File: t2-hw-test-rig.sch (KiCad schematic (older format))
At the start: 36 parts

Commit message: annotated
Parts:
- gave numbers to parts that had none: 36

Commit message: annotated, netlist
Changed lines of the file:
@@
 $EndComp
 $Comp
-L GND #PWR110
+L GND #PWR01
 U 1 1 5530823B
 P 5100 7500
-F 0 "#PWR110" H 5100 7250 50  0001 C CNN
+F 0 "#PWR01" H 5100 7250 50  0001 C CNN
 F 1 "GND" H 5100 7350 50  0000 C CNN
 F 2 "" H 5100 7500 60  0000 C CNN
@@
 $EndComp
 $Comp
-L GND #PWR104
+L GND #PWR02
 U 1 1 553082CD
 P 3500 7500
-F 0 "#PWR104" H 3500 7250 50  0001 C CNN
+F 0 "#PWR02" H 3500 7250 50  0001 C CNN
 F 1 "GND" H 3500 7350 50  0000 C CNN
 F 2 "" H 3500 7500 60  0000 C CNN
@@
 $EndComp
 $Comp
-L GND #PWR106
+L GND #PWR03
 U 1 1 55308387
 P 3900 7000
-F 0 "#PWR106" H 3900 6750 50  0001 C CNN
+F 0 "#PWR03" H 3900 6750 50  0001 C CNN
 F 1 "GND" H 3900 6850 50  0000 C CNN
 F 2 "" H 3900 7000 60  0000 C CNN
@@
 $EndComp
 $Comp
-L GND #PWR108
+L GND #PWR04
 U 1 1 5530B320
 P 4400 5200
-F 0 "#PWR108" H 4400 4950 50  0001 C CNN
+F 0 "#PWR04" H 4400 4950 50  0001 C CNN
 F 1 "GND" H 4400 5050 50  0000 C CNN
 F 2 "" H 4400 5200 60  0000 C CNN
@@
 $EndComp
 $Comp
-L +5V #PWR101
+L +5V #PWR05
 U 1 1 5530BC5F
 P 3300 4800
-F 0 "#PWR101" H 3300 4650 50  0001 C CNN
+F 0 "#PWR05" H 3300 4650 50  0001 C CNN
 F 1 "+5V" H 3300 4940 50  0000 C CNN
 F 2 "" H 3300 4800 60  0000 C CNN
@@
 $EndComp
 $Comp
-L GND #PWR105
+L GND #PWR06
 U 1 1 5530C144
 P 3900 5700
-F 0 "#PWR105" H 3900 5450 50  0001 C CNN
+F 0 "#PWR06" H 3900 5450 50  0001 C CNN
 F 1 "GND" H 3900 5550 50  0000 C CNN
 F 2 "" H 3900 5700 60  0000 C CNN
@@
 $EndComp
 $Comp
-L GND #PWR103
+L GND #PWR07
 U 1 1 5530C207
 P 3500 5700
-F 0 "#PWR103" H 3500 5450 50  0001 C CNN
+F 0 "#PWR07" H 3500 5450 50  0001 C CNN
 F 1 "GND" H 3500 5550 50  0000 C CNN
 F 2 "" H 3500 5700 60  0000 C CNN
@@
 $EndComp
 $Comp
-L GND #PWR112
+L GND #PWR08
 U 1 1 5530C2A7
 P 6000 5700
-F 0 "#PWR112" H 6000 5450 50  0001 C CNN
+F 0 "#PWR08" H 6000 5450 50  0001 C CNN
 F 1 "GND" H 6000 5550 50  0000 C CNN
 F 2 "" H 6000 5700 60  0000 C CNN
@@
 $EndComp
 $Comp
-L +3.3V #PWR113
+L +3.3V #PWR09
 U 1 1 5530C581
 P 6300 4800
-F 0 "#PWR113" H 6300 4650 50  0001 C CNN
+F 0 "#PWR09" H 6300 4650 50  0001 C CNN
 F 1 "+3.3V" H 6300 4940 50  0000 C CNN
 F 2 "" H 6300 4800 60  0000 C CNN
@@
 $EndComp
 $Comp
-L +5V #PWR102
+L +5V #PWR010
 U 1 1 5536D76C
 P 3300 6600
-F 0 "#PWR102" H 3300 6450 50  0001 C CNN
+F 0 "#PWR010" H 3300 6450 50  0001 C CNN
 F 1 "+5V" H 3300 6740 50  0000 C CNN
 F 2 "" H 3300 6600 60  0000 C CNN
@@
 $EndComp
 $Comp
-L GND #PWR109
+L GND #PWR011
 U 1 1 5537EEAC
 P 5000 4000
-F 0 "#PWR109" H 5000 3750 50  0001 C CNN
+F 0 "#PWR011" H 5000 3750 50  0001 C CNN
 F 1 "GND" H 5000 3850 50  0000 C CNN
 F 2 "" H 5000 4000 60  0000 C CNN
@@
 $EndComp
 $Comp
-L +5V #PWR111
+L +5V #PWR012
 U 1 1 5537EEF8
 P 5400 2600
-F 0 "#PWR111" H 5400 2450 50  0001 C CNN
+F 0 "#PWR012" H 5400 2450 50  0001 C CNN
 F 1 "+5V" H 5400 2740 50  0000 C CNN
 F 2 "" H 5400 2600 60  0000 C CNN
@@
 	3500 6700 3500 6800
 Wire Wire Line
-	5000 6700 5100 6700
-Wire Wire Line
-	5100 6700 5300 6700
+	5000 6700 5300 6700
 Connection ~ 5100 6700
 Wire Wire Line
-	3300 6700 3500 6700
-Wire Wire Line
-	3500 6700 4000 6700
+	3300 6700 4000 6700
 Wire Wire Line
 	3900 7000 3900 6900
@@
 Connection ~ 3500 6700
 Wire Wire Line
-	3300 4900 3500 4900
-Wire Wire Line
-	3500 4900 3900 4900
-Wire Wire Line
-	3900 4900 4500 4900
+	3300 4900 4500 4900
 Wire Wire Line
 	3300 4900 3300 4800
 Wire Wire Line
-	5900 4900 6000 4900
-Wire Wire Line
-	6000 4900 6300 4900
+	5900 4900 6300 4900
 Wire Wire Line
 	4400 5200 4400 5100
@@
 	3300 6700 3300 6600
 Wire Wire Line
-	4200 3500 4400 3500
-Wire Wire Line
-	4400 3500 4800 3500
+	4200 3500 4800 3500
 Wire Wire Line
 	5400 3500 5200 3500
 Wire Wire Line
-	5400 2600 5400 2800
-Wire Wire Line
-	5400 2800 5400 3500
-Wire Wire Line
-	5000 3800 5000 3900
-Wire Wire Line
-	5000 3900 5000 4000
+	5400 2600 5400 3500
+Wire Wire Line
+	5000 3800 5000 4000
 Wire Wire Line
 	4200 3600 4300 3600
 Wire Wire Line
-	4300 3600 4300 3700
-Wire Wire Line
-	4300 3700 4300 3900
+	4300 3600 4300 3900
 Wire Wire Line
 	4300 3700 4200 3700
@@
 Connection ~ 4300 3700
 Wire Wire Line
-	4000 2800 4400 2800
-Wire Wire Line
-	4400 2800 4900 2800
+	4000 2800 4900 2800
 Wire Wire Line
 	4400 2800 4400 3500
 Connection ~ 4400 3500
 $Comp
-L GND #PWR107
+L GND #PWR013
 U 1 1 5537FB7D
 P 4100 3000
-F 0 "#PWR107" H 4100 2750 50  0001 C CNN
+F 0 "#PWR013" H 4100 2750 50  0001 C CNN
 F 1 "GND" H 4100 2850 50  0000 C CNN
 F 2 "" H 4100 3000 60  0000 C CNN

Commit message: components and footprints
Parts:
- C101: footprint (none) -> tm-kicad-lib:SMD-0805-C
- C102, C103, C104, C105: footprint (none) -> tm-kicad-lib:SMD-0402-C
- H101, H102, H103, H104: footprint (none) -> tm-kicad-lib:MountingHole_2-5mm
- J101, J103: footprint (none) -> Pin_Headers:Pin_Header_Straight_1x02
- J102: footprint (none) -> Connect:BARREL_JACK
- Q101: footprint FOOTPRINT -> Housings_SOT-23_SOT-143_TSOT-6:SOT-23
- U101, U102: footprint (none) -> Housings_SOT-23_SOT-143_TSOT-6:SOT-23
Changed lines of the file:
@@
 F 0 "C104" H 5125 7200 50  0000 L CNN
 F 1 "100nF" H 5125 7000 50  0000 L CNN
-F 2 "" H 5138 6950 30  0000 C CNN
+F 2 "tm-kicad-lib:SMD-0402-C" H 5138 6950 30  0001 C CNN
 F 3 "" H 5100 7100 60  0000 C CNN
 	1    5100 7100
@@
 F 0 "C102" H 3525 7200 50  0000 L CNN
 F 1 "100nF" H 3525 7000 50  0000 L CNN
-F 2 "" H 3538 6950 30  0000 C CNN
+F 2 "tm-kicad-lib:SMD-0402-C" H 3538 6950 30  0001 C CNN
 F 3 "" H 3500 7100 60  0000 C CNN
 	1    3500 7100
@@
 F 0 "U101" H 4300 7050 60  0000 C CNN
 F 1 "MAX6102" H 4500 6800 60  0000 C CNN
-F 2 "" H 4500 6800 60  0000 C CNN
+F 2 "Housings_SOT-23_SOT-143_TSOT-6:SOT-23" H 4500 6800 60  0001 C CNN
 F 3 "" H 4500 6800 60  0000 C CNN
 	1    4500 6800
@@
 F 0 "U102" H 4800 5250 60  0000 C CNN
 F 1 "XC6206P332MR-G" H 5200 5000 60  0000 C CNN
-F 2 "" H 5200 5000 60  0000 C CNN
+F 2 "Housings_SOT-23_SOT-143_TSOT-6:SOT-23" H 5200 5000 60  0001 C CNN
 F 3 "" H 5200 5000 60  0000 C CNN
 	1    5200 5000
@@
 F 0 "C103" H 3925 5400 50  0000 L CNN
 F 1 "100nF" H 3925 5200 50  0000 L CNN
-F 2 "" H 3938 5150 30  0000 C CNN
+F 2 "tm-kicad-lib:SMD-0402-C" H 3938 5150 30  0001 C CNN
 F 3 "" H 3900 5300 60  0000 C CNN
 	1    3900 5300
@@
 F 0 "C101" H 3525 5400 50  0000 L CNN
 F 1 "10uF" H 3525 5200 50  0000 L CNN
-F 2 "" H 3538 5150 30  0000 C CNN
+F 2 "tm-kicad-lib:SMD-0805-C" H 3538 5150 30  0001 C CNN
 F 3 "" H 3500 5300 60  0000 C CNN
 	1    3500 5300
@@
 F 0 "C105" H 6025 5400 50  0000 L CNN
 F 1 "100nF" H 6025 5200 50  0000 L CNN
-F 2 "" H 6038 5150 30  0000 C CNN
+F 2 "tm-kicad-lib:SMD-0402-C" H 6038 5150 30  0001 C CNN
 F 3 "" H 6000 5300 60  0000 C CNN
 	1    6000 5300
@@
 F 0 "J102" H 3900 3850 60  0000 C CNN
 F 1 "BARREL_JACK" H 3900 3400 60  0000 C CNN
-F 2 "" H 3900 3600 60  0000 C CNN
+F 2 "Connect:BARREL_JACK" H 3900 3600 60  0001 C CNN
 F 3 "" H 3900 3600 60  0000 C CNN
 	1    3900 3600
@@
 F 0 "Q101" V 5350 3600 40  0000 C CNN
 F 1 "pMOS" V 5250 3600 40  0000 C CNN
-F 2 "FOOTPRINT" H 4800 3650 29  0001 C CNN
+F 2 "Housings_SOT-23_SOT-143_TSOT-6:SOT-23" H 4800 3650 29  0001 C CNN
 F 3 "" H 5000 3600 60  0000 C CNN
 	1    5000 3600
@@
 F 0 "J101" H 3800 3000 50  0000 C CNN
 F 1 "CONN_01X02" V 3900 2850 50  0000 C CNN
-F 2 "" H 3800 2850 60  0000 C CNN
+F 2 "Pin_Headers:Pin_Header_Straight_1x02" H 3800 2850 60  0001 C CNN
 F 3 "" H 3800 2850 60  0000 C CNN
 	1    3800 2850
@@
 F 0 "J103" H 4950 2650 50  0000 C CNN
 F 1 "CONN_01X02" V 5050 2500 50  0000 C CNN
-F 2 "" H 4950 2500 60  0000 C CNN
+F 2 "Pin_Headers:Pin_Header_Straight_1x02" H 4950 2500 60  0001 C CNN
 F 3 "" H 4950 2500 60  0000 C CNN
 	1    4950 2500
@@
 F 0 "JP101" H 4800 2350 50  0000 C CNN
 F 1 "JUMPER" H 4800 2120 50  0000 C CNN
-F 2 "" H 4800 2200 60  0000 C CNN
+F 2 "" H 4800 2200 60  0001 C CNN
 F 3 "" H 4800 2200 60  0000 C CNN
 	1    4800 2200
@@
 F 0 "P102" H 9550 2450 50  0000 C CNN
 F 1 "USB A TO MicroUSB A CABLE" H 10200 2200 50  0000 C CNN
-F 2 "" H 9550 2200 60  0000 C CNN
+F 2 "" H 9550 2200 60  0001 C CNN
 F 3 "" H 9550 2200 60  0000 C CNN
 	1    9550 2200
@@
 F 0 "P103" H 11700 3600 50  0000 C CNN
 F 1 "USB A TO MicroUSB A CABLE" H 12350 3350 50  0000 C CNN
-F 2 "" H 11700 3350 60  0000 C CNN
+F 2 "" H 11700 3350 60  0001 C CNN
 F 3 "" H 11700 3350 60  0000 C CNN
 	1    11700 3350
@@
 F 0 "P104" H 12650 2750 50  0000 C CNN
 F 1 "ETHERNET CABLE" H 13050 2300 50  0000 C CNN
-F 2 "" H 12650 2300 60  0000 C CNN
+F 2 "" H 12650 2300 60  0001 C CNN
 F 3 "" H 12650 2300 60  0000 C CNN
 	1    12650 2300
@@
 F 0 "P101" H 2900 3700 50  0000 C CNN
 F 1 "5VDC POWER" H 3250 3550 50  0000 C CNN
-F 2 "" H 2900 3550 60  0000 C CNN
+F 2 "" H 2900 3550 60  0001 C CNN
 F 3 "" H 2900 3550 60  0000 C CNN
 	1    2900 3550
@@
 F 0 "P105" H 13700 3300 50  0000 C CNN
 F 1 "USB THUMB DRIVE" H 14150 3050 50  0000 C CNN
-F 2 "" H 13700 3050 60  0000 C CNN
+F 2 "" H 13700 3050 60  0001 C CNN
 F 3 "" H 13700 3050 60  0000 C CNN
 	1    13700 3050
@@
 F 0 "P106" H 13700 3800 50  0000 C CNN
 F 1 "USB THUMB DRIVE" H 14150 3550 50  0000 C CNN
-F 2 "" H 13700 3550 60  0000 C CNN
+F 2 "" H 13700 3550 60  0001 C CNN
 F 3 "" H 13700 3550 60  0000 C CNN
 	1    13700 3550
@@
 F 0 "H101" H 7100 7900 60  0000 C CNN
 F 1 "M2.5" H 7100 7600 60  0000 C CNN
-F 2 "" H 7100 7750 60  0000 C CNN
+F 2 "tm-kicad-lib:MountingHole_2-5mm" H 7100 7750 60  0001 C CNN
 F 3 "" H 7100 7750 60  0000 C CNN
 	1    7100 7750
@@
 F 0 "H102" H 7700 7900 60  0000 C CNN
 F 1 "M2.5" H 7700 7600 60  0000 C CNN
-F 2 "" H 7700 7750 60  0000 C CNN
+F 2 "tm-kicad-lib:MountingHole_2-5mm" H 7700 7750 60  0001 C CNN
 F 3 "" H 7700 7750 60  0000 C CNN
 	1    7700 7750
@@
 F 0 "H103" H 8300 7900 60  0000 C CNN
 F 1 "M2.5" H 8300 7600 60  0000 C CNN
-F 2 "" H 8300 7750 60  0000 C CNN
+F 2 "tm-kicad-lib:MountingHole_2-5mm" H 8300 7750 60  0001 C CNN
 F 3 "" H 8300 7750 60  0000 C CNN
 	1    8300 7750
@@
 F 0 "H104" H 8900 7900 60  0000 C CNN
 F 1 "M2.5" H 8900 7600 60  0000 C CNN
-F 2 "" H 8900 7750 60  0000 C CNN
+F 2 "tm-kicad-lib:MountingHole_2-5mm" H 8900 7750 60  0001 C CNN
 F 3 "" H 8900 7750 60  0000 C CNN
 	1    8900 7750
@@
 F 0 "MP101" H 7100 6800 60  0000 C CNN
 F 1 "98952A202" H 7100 7200 60  0000 C CNN
-F 2 "" H 7100 7200 60  0000 C CNN
+F 2 "" H 7100 7200 60  0001 C CNN
 F 3 "" H 7100 7200 60  0000 C CNN
 	1    7100 7100
@@
 F 0 "MP102" H 7100 8200 60  0000 C CNN
 F 1 "98952A209" H 7100 8600 60  0000 C CNN
-F 2 "" H 7100 8600 60  0000 C CNN
+F 2 "" H 7100 8600 60  0001 C CNN
 F 3 "" H 7100 8600 60  0000 C CNN
 	1    7100 8500
@@
 F 0 "MP105" H 7700 6800 60  0000 C CNN
 F 1 "98952A202" H 7700 7200 60  0000 C CNN
-F 2 "" H 7700 7200 60  0000 C CNN
+F 2 "" H 7700 7200 60  0001 C CNN
 F 3 "" H 7700 7200 60  0000 C CNN
 	1    7700 7100
@@
 F 0 "MP106" H 7700 8200 60  0000 C CNN
 F 1 "98952A209" H 7700 8600 60  0000 C CNN
-F 2 "" H 7700 8600 60  0000 C CNN
+F 2 "" H 7700 8600 60  0001 C CNN
 F 3 "" H 7700 8600 60  0000 C CNN
 	1    7700 8500
@@
 F 0 "MP108" H 8300 6800 60  0000 C CNN
 F 1 "98952A202" H 8300 7200 60  0000 C CNN
-F 2 "" H 8300 7200 60  0000 C CNN
+F 2 "" H 8300 7200 60  0001 C CNN
 F 3 "" H 8300 7200 60  0000 C CNN
 	1    8300 7100
@@
 F 0 "MP109" H 8300 8200 60  0000 C CNN
 F 1 "98952A209" H 8300 8600 60  0000 C CNN
-F 2 "" H 8300 8600 60  0000 C CNN
+F 2 "" H 8300 8600 60  0001 C CNN
 F 3 "" H 8300 8600 60  0000 C CNN
 	1    8300 8500
@@
 F 0 "MP111" H 8900 6800 60  0000 C CNN
 F 1 "98952A202" H 8900 7200 60  0000 C CNN
-F 2 "" H 8900 7200 60  0000 C CNN
+F 2 "" H 8900 7200 60  0001 C CNN
 F 3 "" H 8900 7200 60  0000 C CNN
 	1    8900 7100
@@
 F 0 "MP112" H 8900 8200 60  0000 C CNN
 F 1 "98952A209" H 8900 8600 60  0000 C CNN
-F 2 "" H 8900 8600 60  0000 C CNN
+F 2 "" H 8900 8600 60  0001 C CNN
 F 3 "" H 8900 8600 60  0000 C CNN
 	1    8900 8500
@@
 F 0 "MP103" H 7100 9200 60  0000 C CNN
 F 1 "PLATE" H 7100 8800 60  0000 C CNN
-F 2 "" H 7100 9200 60  0000 C CNN
+F 2 "" H 7100 9200 60  0001 C CNN
 F 3 "" H 7100 9200 60  0000 C CNN
 	1    7100 9100
@@
 F 0 "MP104" H 7100 9700 60  0000 C CNN
 F 1 "92290A060" H 7100 10100 60  0000 C CNN
-F 2 "" H 7100 10100 60  0000 C CNN
+F 2 "" H 7100 10100 60  0001 C CNN
 F 3 "" H 7100 10100 60  0000 C CNN
 	1    7100 10000
@@
 F 0 "MP114" H 9700 8400 60  0000 C CNN
 F 1 "201B" H 9700 8000 60  0000 C CNN
-F 2 "" H 9700 8400 60  0000 C CNN
+F 2 "" H 9700 8400 60  0001 C CNN
 F 3 "" H 9700 8400 60  0000 C CNN
 	1    9700 8300
@@
 F 0 "MP107" H 7700 9700 60  0000 C CNN
 F 1 "92290A060" H 7700 10100 60  0000 C CNN
-F 2 "" H 7700 10100 60  0000 C CNN
+F 2 "" H 7700 10100 60  0001 C CNN
 F 3 "" H 7700 10100 60  0000 C CNN
 	1    7700 10000
@@
 F 0 "MP110" H 8300 9700 60  0000 C CNN
 F 1 "92290A060" H 8300 10100 60  0000 C CNN
-F 2 "" H 8300 10100 60  0000 C CNN
+F 2 "" H 8300 10100 60  0001 C CNN
 F 3 "" H 8300 10100 60  0000 C CNN
 	1    8300 10000
@@
 F 0 "MP113" H 8900 9700 60  0000 C CNN
 F 1 "92290A060" H 8900 10100 60  0000 C CNN
-F 2 "" H 8900 10100 60  0000 C CNN
+F 2 "" H 8900 10100 60  0001 C CNN
 F 3 "" H 8900 10100 60  0000 C CNN
 	1    8900 10000

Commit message: on to layout! and what an adventure it will be...
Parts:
- added H105, H106: M2.5, tm-kicad-lib:MountingHole_2-5mm, symbol HOLE
- added MP115, MP118: 98952A209, symbol MECHANICAL
- added MP116, MP119: 92290A060, symbol MECHANICAL
- added MP117, MP120: 90592A006, symbol MECHANICAL
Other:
- note added: "M2.5 HEX NUTS"
- moved on the sheet: MP114
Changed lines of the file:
@@
 L MECHANICAL MP114
 U 1 1 55451CE8
-P 9700 8300
-F 0 "MP114" H 9700 8400 60  0000 C CNN
-F 1 "201B" H 9700 8000 60  0000 C CNN
-F 2 "" H 9700 8400 60  0001 C CNN
-F 3 "" H 9700 8400 60  0000 C CNN
-	1    9700 8300
+P 10900 8300
+F 0 "MP114" H 10900 8400 60  0000 C CNN
+F 1 "201B" H 10900 8000 60  0000 C CNN
+F 2 "" H 10900 8400 60  0001 C CNN
+F 3 "" H 10900 8400 60  0000 C CNN
+	1    10900 8300
 	1    0    0    -1
 $EndComp
-Text Notes 9500 8100 0    60   ~ 0
+Text Notes 10700 8100 0    60   ~ 0
 TOGGLE CLAMP ASSEMBLY
 Text Notes 6800 7500 0    60   ~ 0
@@
 Text Notes 7200 6300 0    60   ~ 0
 RIG STACKUP/ASSEMBLY:
-Text Notes 10000 8500 0    60   ~ 0
+Text Notes 11200 8500 0    60   ~ 0
 ADDITIONAL HARDWARE\nMAY BE NECESSARY FOR\nTOGGLE CLAMP MOUNTING
 $Comp
@@
 	1    0    0    1
 $EndComp
+$Comp
+L HOLE H105
+U 1 1 5547EFD9
+P 9500 7750
+F 0 "H105" H 9500 7900 60  0000 C CNN
+F 1 "M2.5" H 9500 7600 60  0000 C CNN
+F 2 "tm-kicad-lib:MountingHole_2-5mm" H 9500 7750 60  0001 C CNN
+F 3 "" H 9500 7750 60  0000 C CNN
+	1    9500 7750
+	1    0    0    -1
+$EndComp
+$Comp
+L HOLE H106
+U 1 1 5547EFDF
+P 10100 7750
+F 0 "H106" H 10100 7900 60  0000 C CNN
+F 1 "M2.5" H 10100 7600 60  0000 C CNN
+F 2 "tm-kicad-lib:MountingHole_2-5mm" H 10100 7750 60  0001 C CNN
+F 3 "" H 10100 7750 60  0000 C CNN
+	1    10100 7750
+	1    0    0    -1
+$EndComp
+$Comp
+L MECHANICAL MP115
+U 1 1 5547F398
+P 9500 8500
+F 0 "MP115" H 9500 8200 60  0000 C CNN
+F 1 "98952A209" H 9500 8600 60  0000 C CNN
+F 2 "" H 9500 8600 60  0001 C CNN
+F 3 "" H 9500 8600 60  0000 C CNN
+	1    9500 8500
+	1    0    0    1
+$EndComp
+$Comp
+L MECHANICAL MP118
+U 1 1 5547F39E
+P 10100 8500
+F 0 "MP118" H 10100 8200 60  0000 C CNN
+F 1 "98952A209" H 10100 8600 60  0000 C CNN
+F 2 "" H 10100 8600 60  0001 C CNN
+F 3 "" H 10100 8600 60  0000 C CNN
+	1    10100 8500
+	1    0    0    1
+$EndComp
+$Comp
+L MECHANICAL MP116
+U 1 1 5547F44C
+P 9500 10000
+F 0 "MP116" H 9500 9700 60  0000 C CNN
+F 1 "92290A060" H 9500 10100 60  0000 C CNN
+F 2 "" H 9500 10100 60  0001 C CNN
+F 3 "" H 9500 10100 60  0000 C CNN
+	1    9500 10000
+	1    0    0    1
+$EndComp
+$Comp
+L MECHANICAL MP119
+U 1 1 5547F452
+P 10100 10000
+F 0 "MP119" H 10100 9700 60  0000 C CNN
+F 1 "92290A060" H 10100 10100 60  0000 C CNN
+F 2 "" H 10100 10100 60  0001 C CNN
+F 3 "" H 10100 10100 60  0000 C CNN
+	1    10100 10000
+	1    0    0    1
+$EndComp
+$Comp
+L MECHANICAL MP117
+U 1 1 5547F5EC
+P 9800 7100
+F 0 "MP117" H 9800 6800 60  0000 C CNN
+F 1 "90592A006" H 9800 7200 60  0000 C CNN
+F 2 "" H 9800 7200 60  0001 C CNN
+F 3 "" H 9800 7200 60  0000 C CNN
+	1    9800 7100
+	1    0    0    1
+$EndComp
+Text Notes 9500 6700 0    60   ~ 0
+M2.5 HEX NUTS
+$Comp
+L MECHANICAL MP120
+U 1 1 5547F832
+P 10400 7100
+F 0 "MP120" H 10400 6800 60  0000 C CNN
+F 1 "90592A006" H 10400 7200 60  0000 C CNN
+F 2 "" H 10400 7200 60  0001 C CNN
+F 3 "" H 10400 7200 60  0000 C CNN
+	1    10400 7100
+	1    0    0    1
+$EndComp

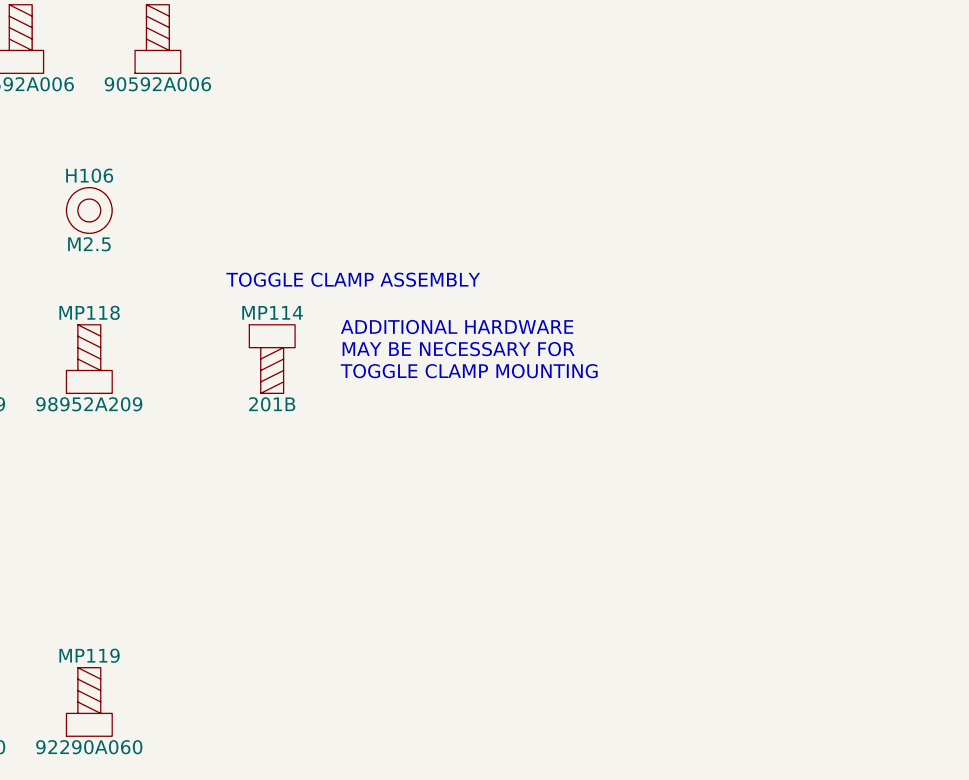
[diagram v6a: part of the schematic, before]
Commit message: usb refactor on sch and pcb, mechanical constraints on bcp
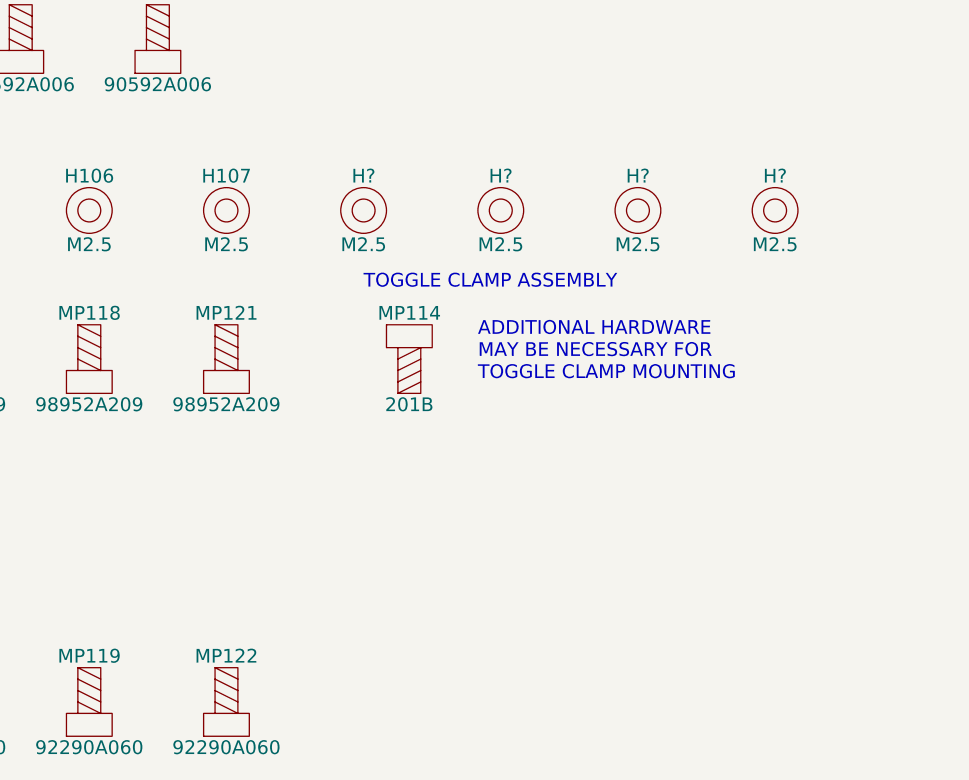
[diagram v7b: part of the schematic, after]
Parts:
- added H107, H? (x4): M2.5, tm-kicad-lib:MountingHole_2-5mm, symbol HOLE
- added MP121: 98952A209, symbol MECHANICAL
- added MP122: 92290A060, symbol MECHANICAL
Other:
- moved on the sheet: MP114
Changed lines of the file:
@@
 L MECHANICAL MP114
 U 1 1 55451CE8
-P 10900 8300
-F 0 "MP114" H 10900 8400 60  0000 C CNN
-F 1 "201B" H 10900 8000 60  0000 C CNN
-F 2 "" H 10900 8400 60  0001 C CNN
-F 3 "" H 10900 8400 60  0000 C CNN
-	1    10900 8300
-	1    0    0    -1
-$EndComp
-Text Notes 10700 8100 0    60   ~ 0
+P 11500 8300
+F 0 "MP114" H 11500 8400 60  0000 C CNN
+F 1 "201B" H 11500 8000 60  0000 C CNN
+F 2 "" H 11500 8400 60  0001 C CNN
+F 3 "" H 11500 8400 60  0000 C CNN
+	1    11500 8300
+	1    0    0    -1
+$EndComp
+Text Notes 11300 8100 0    60   ~ 0
 TOGGLE CLAMP ASSEMBLY
 Text Notes 6800 7500 0    60   ~ 0
@@
 Text Notes 7200 6300 0    60   ~ 0
 RIG STACKUP/ASSEMBLY:
-Text Notes 11200 8500 0    60   ~ 0
+Text Notes 11800 8500 0    60   ~ 0
 ADDITIONAL HARDWARE\nMAY BE NECESSARY FOR\nTOGGLE CLAMP MOUNTING
 $Comp
@@
 	1    0    0    1
 $EndComp
+$Comp
+L HOLE H107
+U 1 1 554A8C39
+P 10700 7750
+F 0 "H107" H 10700 7900 60  0000 C CNN
+F 1 "M2.5" H 10700 7600 60  0000 C CNN
+F 2 "tm-kicad-lib:MountingHole_2-5mm" H 10700 7750 60  0001 C CNN
+F 3 "" H 10700 7750 60  0000 C CNN
+	1    10700 7750
+	1    0    0    -1
+$EndComp
+$Comp
+L MECHANICAL MP121
+U 1 1 554A8C3F
+P 10700 8500
+F 0 "MP121" H 10700 8200 60  0000 C CNN
+F 1 "98952A209" H 10700 8600 60  0000 C CNN
+F 2 "" H 10700 8600 60  0001 C CNN
+F 3 "" H 10700 8600 60  0000 C CNN
+	1    10700 8500
+	1    0    0    1
+$EndComp
+$Comp
+L MECHANICAL MP122
+U 1 1 554A8C45
+P 10700 10000
+F 0 "MP122" H 10700 9700 60  0000 C CNN
+F 1 "92290A060" H 10700 10100 60  0000 C CNN
+F 2 "" H 10700 10100 60  0001 C CNN
+F 3 "" H 10700 10100 60  0000 C CNN
+	1    10700 10000
+	1    0    0    1
+$EndComp
+$Comp
+L HOLE H?
+U 1 1 554A99A8
+P 11300 7750
+F 0 "H?" H 11300 7900 60  0000 C CNN
+F 1 "M2.5" H 11300 7600 60  0000 C CNN
+F 2 "tm-kicad-lib:MountingHole_2-5mm" H 11300 7750 60  0001 C CNN
+F 3 "" H 11300 7750 60  0000 C CNN
+	1    11300 7750
+	1    0    0    -1
+$EndComp
+$Comp
+L HOLE H?
+U 1 1 554A99AE
+P 11900 7750
+F 0 "H?" H 11900 7900 60  0000 C CNN
+F 1 "M2.5" H 11900 7600 60  0000 C CNN
+F 2 "tm-kicad-lib:MountingHole_2-5mm" H 11900 7750 60  0001 C CNN
+F 3 "" H 11900 7750 60  0000 C CNN
+	1    11900 7750
+	1    0    0    -1
+$EndComp
+$Comp
+L HOLE H?
+U 1 1 554A99B4
+P 12500 7750
+F 0 "H?" H 12500 7900 60  0000 C CNN
+F 1 "M2.5" H 12500 7600 60  0000 C CNN
+F 2 "tm-kicad-lib:MountingHole_2-5mm" H 12500 7750 60  0001 C CNN
+F 3 "" H 12500 7750 60  0000 C CNN
+	1    12500 7750
+	1    0    0    -1
+$EndComp
+$Comp
+L HOLE H?
+U 1 1 554A99BA
+P 13100 7750
+F 0 "H?" H 13100 7900 60  0000 C CNN
+F 1 "M2.5" H 13100 7600 60  0000 C CNN
+F 2 "tm-kicad-lib:MountingHole_2-5mm" H 13100 7750 60  0001 C CNN
+F 3 "" H 13100 7750 60  0000 C CNN
+	1    13100 7750
+	1    0    0    -1
+$EndComp
 $EndSCHEMATC
